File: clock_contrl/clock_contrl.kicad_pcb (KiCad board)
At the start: 2 copper layers, 17 parts, among them J1 RJ45, J2 USB_C_Receptacle_PowerOnly_6P, J6 Conn_01x16_Socket, J7 Conn_01x08_Socket, SW1 RotaryEncoder_Switch, SW2 S4_SW_Push, SW3 S3_SW_Push, SW4 S2_SW_Push, SW5 S1_SW_Push, SW6 MODE_SW_Push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

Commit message: 部品の配置を変えてみました
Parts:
- RS485toTTL5V_MAX1348_SH-U12: moved to B.Cu
- moved SW1 160.3 mm to (76.2, 106.7)
- moved SW6 132.6 mm to (96.6, 106.7), turned to 0 degrees
- moved SW5 97.3 mm to (114.4, 106.7), turned to 0 degrees
- moved R1 83.6 mm to (184.1, 119.3)
- moved J2 79.0 mm to (115.5, 76.4)
- moved ? 79.0 mm to (133.2, 62.2)
- moved J6 79.0 mm to (81.2, 120.6)
- moved J7 79.0 mm to (81.2, 97.8)
- moved J1 78.9 mm to (192.7, 114.6)
- moved C1 76.4 mm to (105.4, 90.2), turned to 90 degrees
- moved C2 72.9 mm to (119.2, 90.2)
- moved RS485toTTL5V_MAX1348_SH-U12 72.4 mm to (136.9, 97.5)
- moved U4 64.7 mm to (147.6, 72.9)
- moved SW4 62.4 mm to (132.2, 106.7), turned to 0 degrees
- moved SW3 28.9 mm to (149.9, 106.7), turned to 0 degrees
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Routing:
- net Net-(J6-Pin_21): track 123.1 -> 0.00 mm
- net Net-(J6-Pin_22): track 116.1 -> 0.00 mm
- net Net-(J8-Pin_1): track 71.6 -> 0.00 mm
- net Net-(J11-Pin_2): track 9.68 -> 0.00 mm
- net Net-(C1-Pad1): track 7.67 -> 0.16 mm
- net Net-(J11-Pin_1): track 6.51 -> 0.00 mm

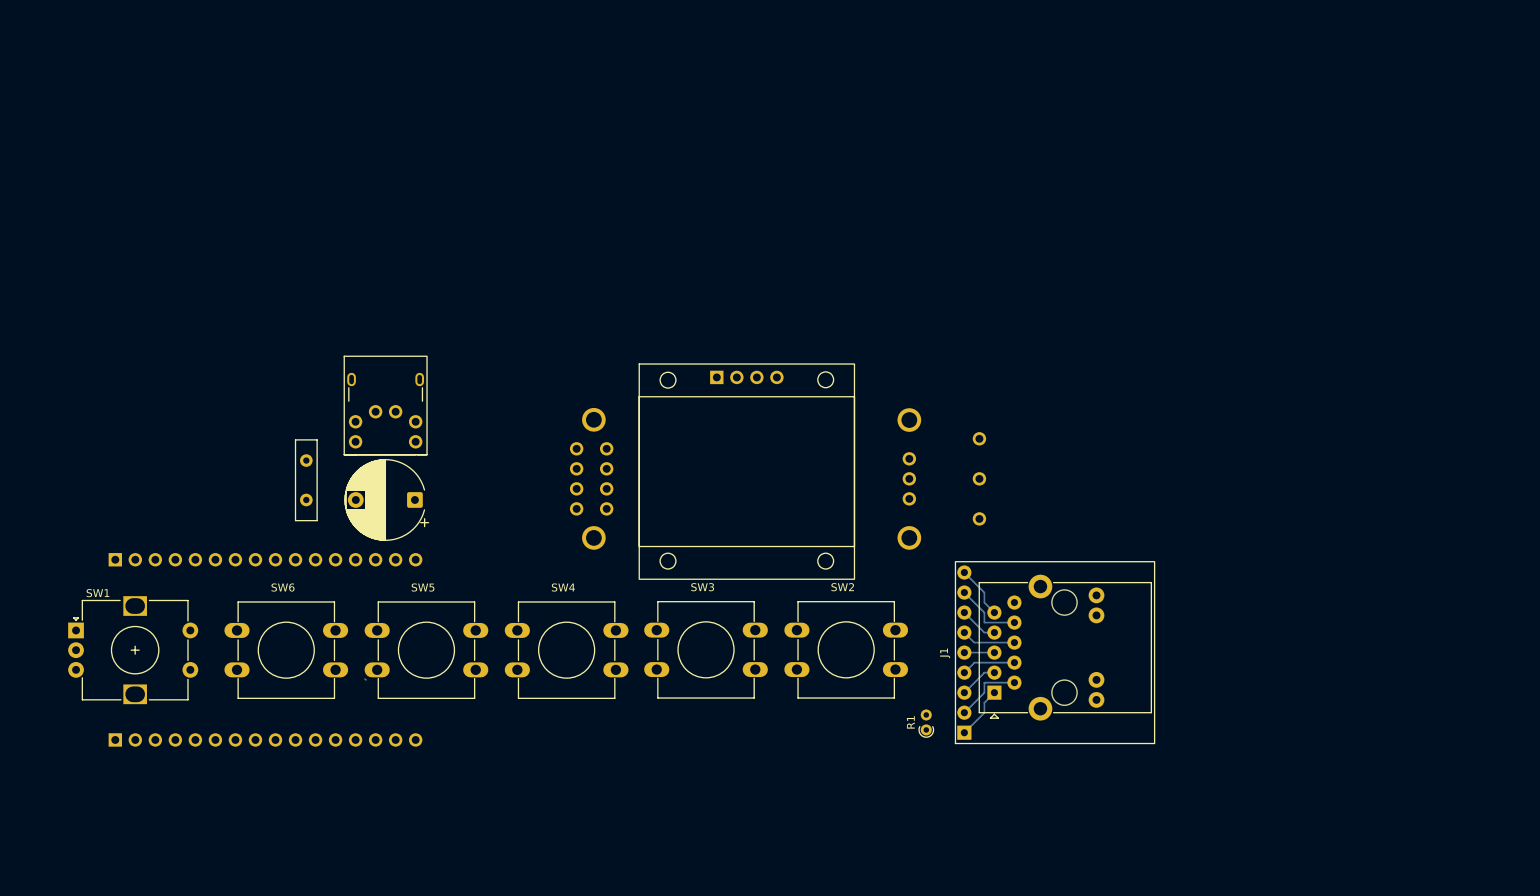
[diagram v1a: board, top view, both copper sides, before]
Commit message: コントロールボックスの基盤を完成しました
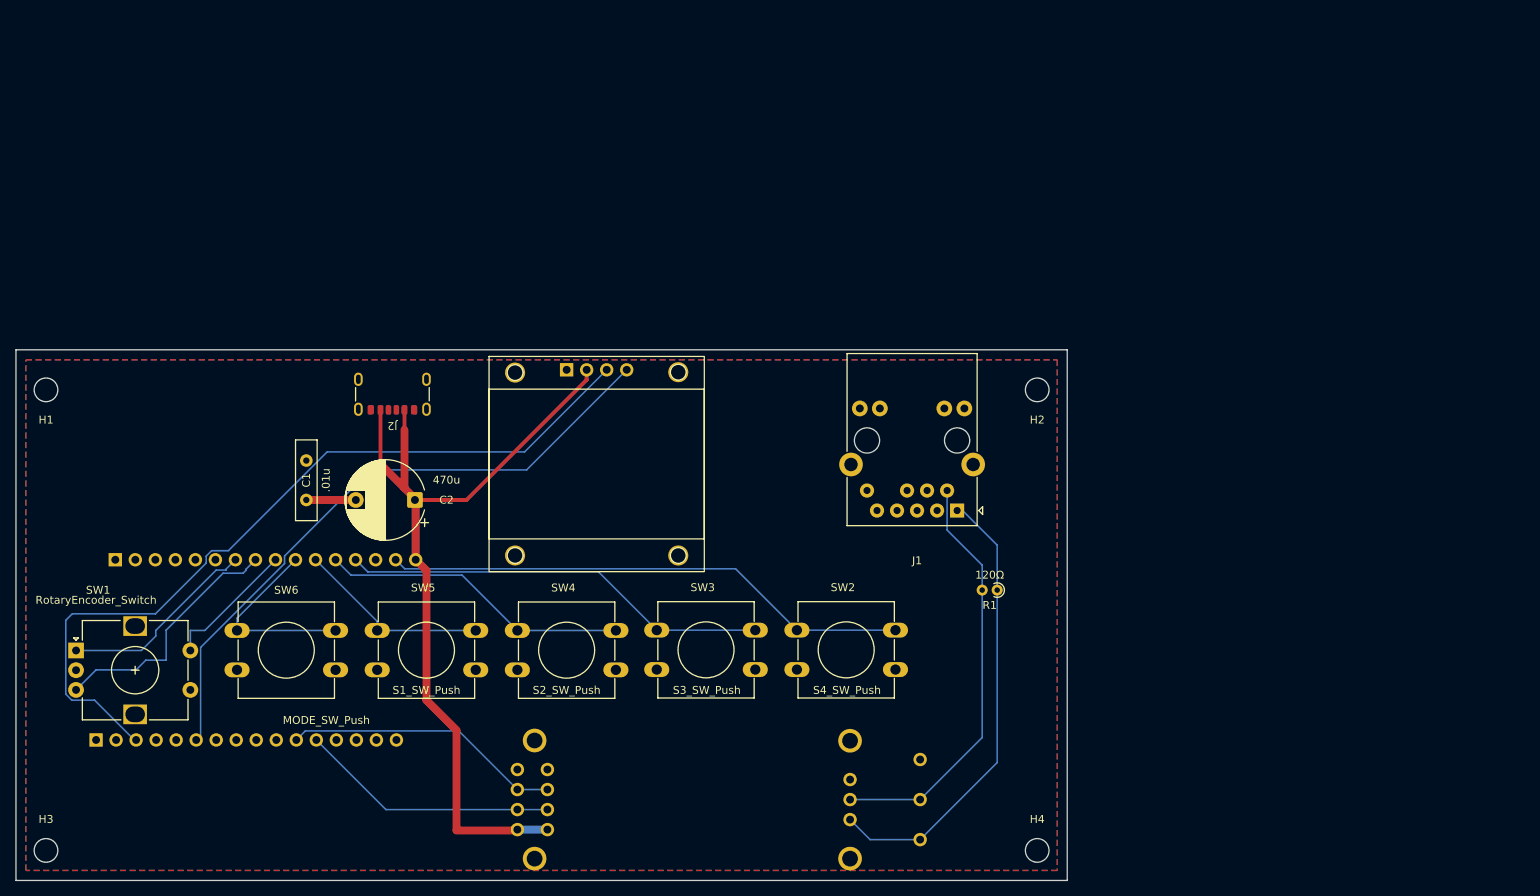
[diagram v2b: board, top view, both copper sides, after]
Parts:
- removed ?: , clipboard:d7bb9d57-0d0f-4d87-902a-f792f1801a50
- added H1: MountingHole, MountingHole:MountingHole_3mm, F.Cu at (72.4, 76.2)
- added H2: MountingHole, MountingHole:MountingHole_3mm, F.Cu at (198.1, 76.2)
- added H3: MountingHole, MountingHole:MountingHole_3mm, F.Cu at (72.4, 134.6)
- added H4: MountingHole, MountingHole:MountingHole_3mm, F.Cu at (198.1, 134.6)
- moved RS485toTTL5V_MAX1348_SH-U12 41.4 mm to (129.3, 138.2)
- moved J1 23.6 mm to (188.0, 91.5), turned to 180 degrees
- moved R1 19.9 mm to (193.0, 101.6), turned to 180 degrees
- moved U4 15.8 mm to (131.9, 74.0)
- moved SW1 2.54 mm to (76.2, 109.3)
- moved J6 2.44 mm to (78.7, 120.6)
- moved J2 1.16 mm to (116.3, 75.7), turned to 180 degrees
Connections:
- C2 pad 1: Net-(J8-Pin_1) -> Net-(U1-VDD)
- J6 pad 0: unconnected-(J6-Pin_0-Pad0) -> (no net)
- J6 pad 15: Net-(J6-Pin_15) -> (no net)
- J6 pad GND: (no net) -> GND
- J7 pad 5V: Net-(J8-Pin_1) -> Net-(U1-VDD)
- J7 pad GND: (no net) -> GND
- RS485toTTL5V_MAX1348_SH-U12 pad 5VO: Net-(J8-Pin_1) -> Net-(U1-VDD)
- U4 pad VCC: Net-(J8-Pin_1) -> Net-(U1-VDD)
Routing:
- net Net-(U1-VDD): track 0.00 -> 108.7 mm
- net /Net-(J6_Pin_22): track 0.00 -> 103.3 mm
- net /Net-(J6_Pin_21): track 0.00 -> 81.2 mm
- net /Net-(J7-Pin_13): track 0.00 -> 67.1 mm
- net Net-(J11-Pin_1): track 0.00 -> 58.2 mm
- net /Net-(J7-Pin_12): track 0.00 -> 54.4 mm
- net Net-(J11-Pin_2): track 0.00 -> 53.2 mm
- net /Net-(J7-Pin_14): track 0.00 -> 39.3 mm
- net Net-(J6-Pin_17): track 0.00 -> 35.4 mm
- net Net-(J6-Pin_16): track 0.00 -> 33.0 mm
- net /Net-(J7-Pin_33): track 0.00 -> 31.9 mm
- net /Net-(J7-Pin_32): track 0.00 -> 25.5 mm
- net /Net-(J7-Pin_27): track 0.00 -> 24.7 mm
- net /Net-(J7-Pin_26): track 0.00 -> 24.5 mm
- net /Net-(J7_Pin_25): track 0.00 -> 17.1 mm
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- added copper zone on B.Cu, net GND
- added copper zone on F.Cu, net GND
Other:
- board outline added: 133.4 x 67.3 mm

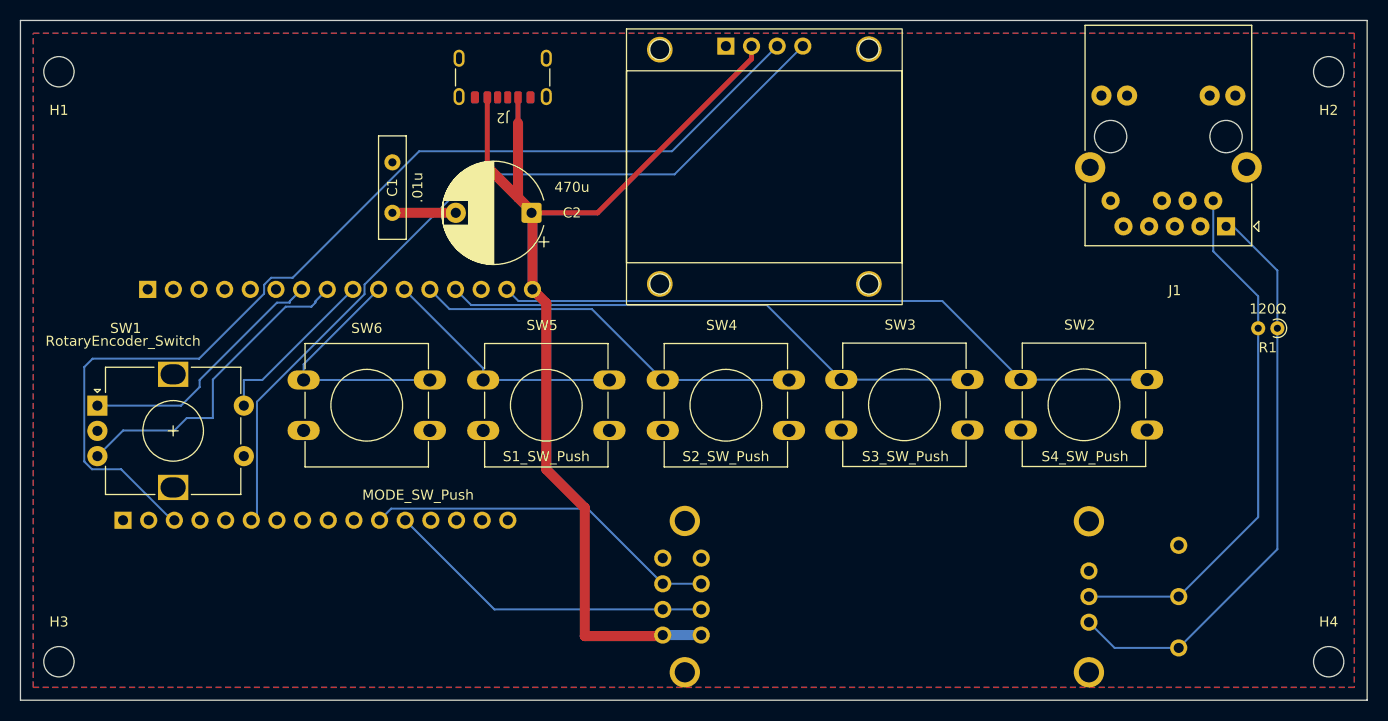
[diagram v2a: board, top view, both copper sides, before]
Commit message: 基盤のUSB端子とRJ45端子を実際のフットプリントに変更しました。
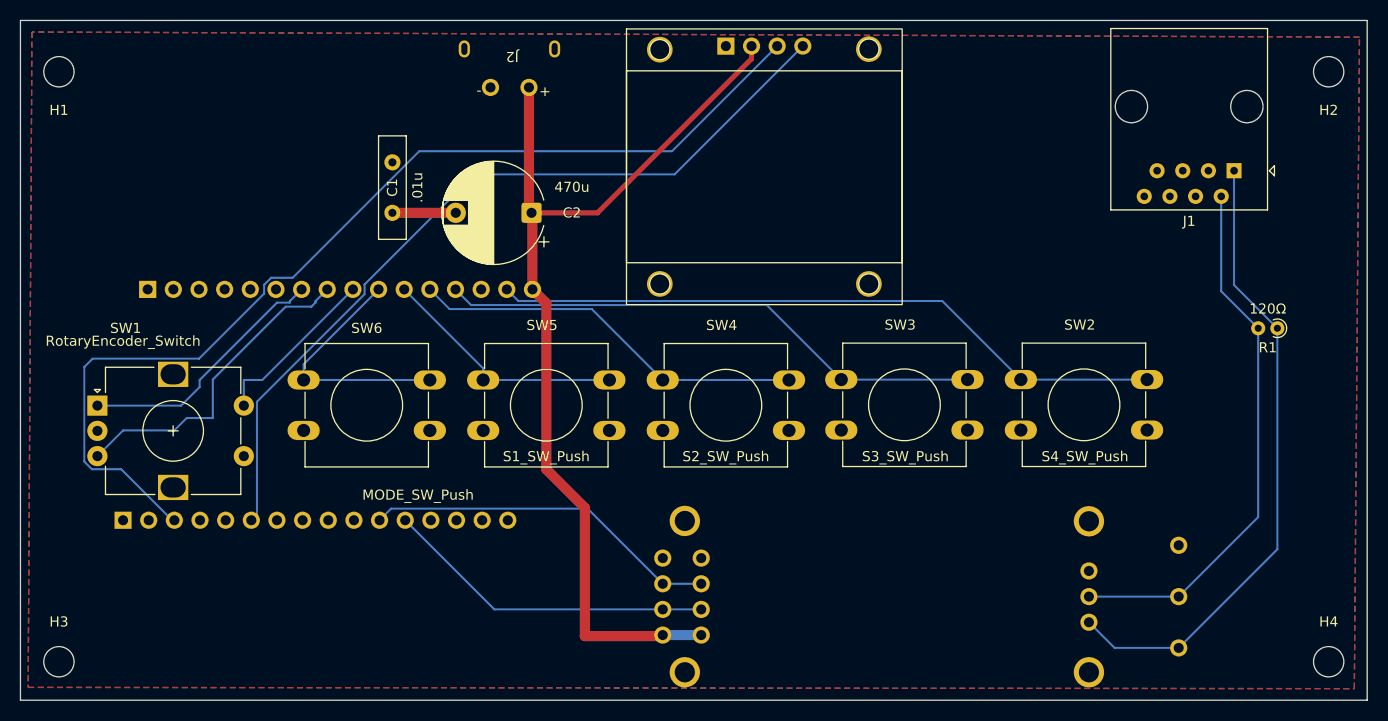
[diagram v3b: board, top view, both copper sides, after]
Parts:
- J1: footprint Connector_RJ:RJ45_Abracon_ARJP11A-MA_Horizontal -> Connector_RJ:RJ45_Amphenol_54602-x08_Horizontal
- moved J1 5.57 mm to (188.8, 86.0)
- moved J2 2.82 mm to (117.0, 72.9)
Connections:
- J2 pad SH: unconnected-(J2-SHIELD-PadSH)_2 -> GND
- J6 pad 15: (no net) -> /Net-(J6_Pin_21)
- U4 pad GND: GND -> (no net)
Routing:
- net Net-(U1-VDD): track 108.7 -> 98.2 mm
- net Net-(J1-Pin1): track 58.2 -> 62.6 mm
